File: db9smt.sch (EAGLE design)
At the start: 20 parts, among them CON1 PADONPRINT, CON2 PADONPRINT, CON3 PADONPRINT, CON4 PADONPRINT, CON5 PADONPRINT, CON6 PADONPRINT, CON7 PADONPRINT, CON8 PADONPRINT, CON9 PADONPRINT

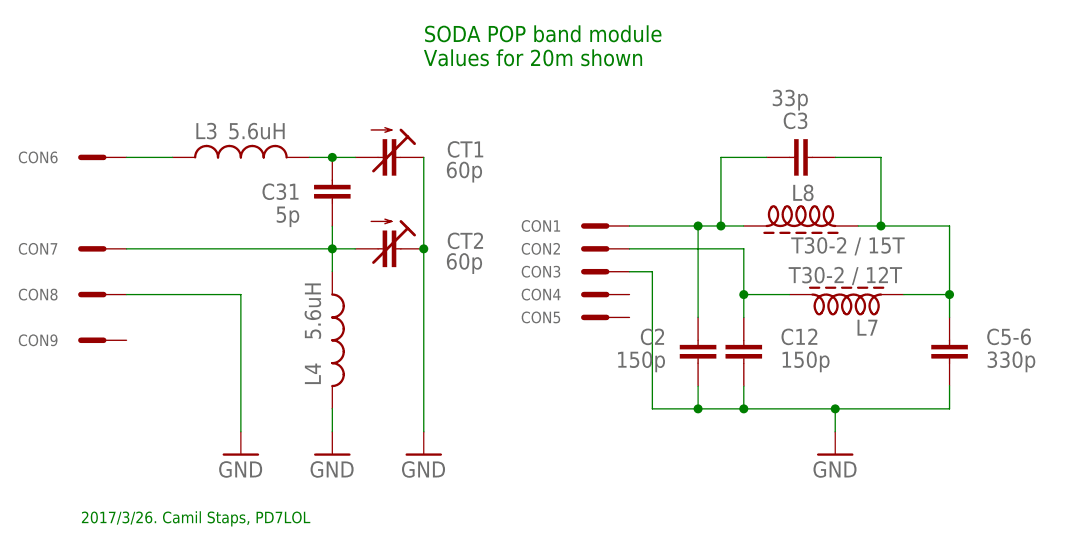
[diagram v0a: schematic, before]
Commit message: GND between signals, remove note space on backside
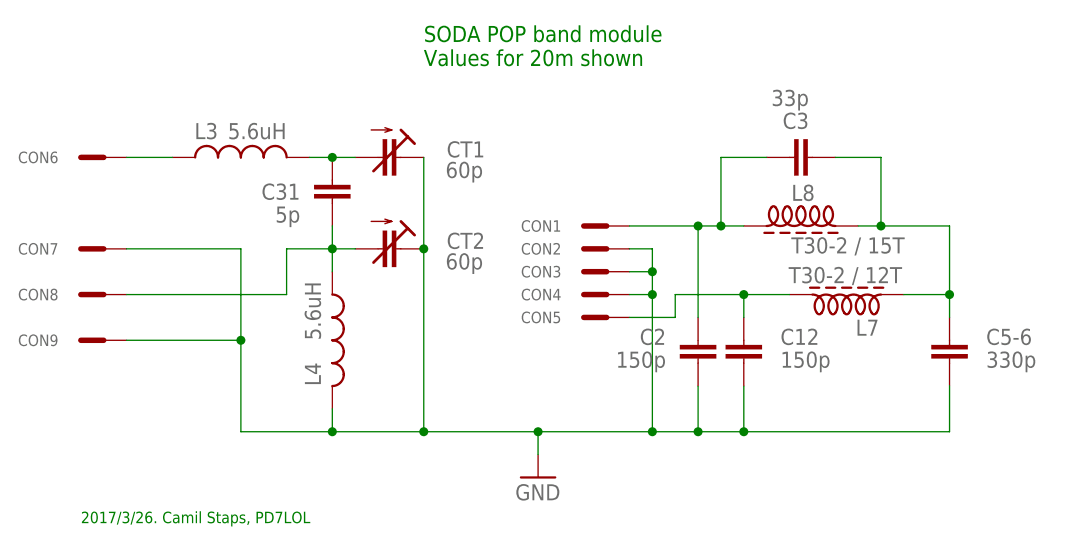
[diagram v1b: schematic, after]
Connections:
- net GND: now also CON2.P$1, CON4.P$1, CON7.P$1, CON9.P$1; no longer CON8.P$1
- net N$1: now also CON8.P$1; no longer CON7.P$1
- net N$5: now also CON5.P$1; no longer CON2.P$1

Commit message: Make DB9 horizontal for smaller footprint and shorter traces
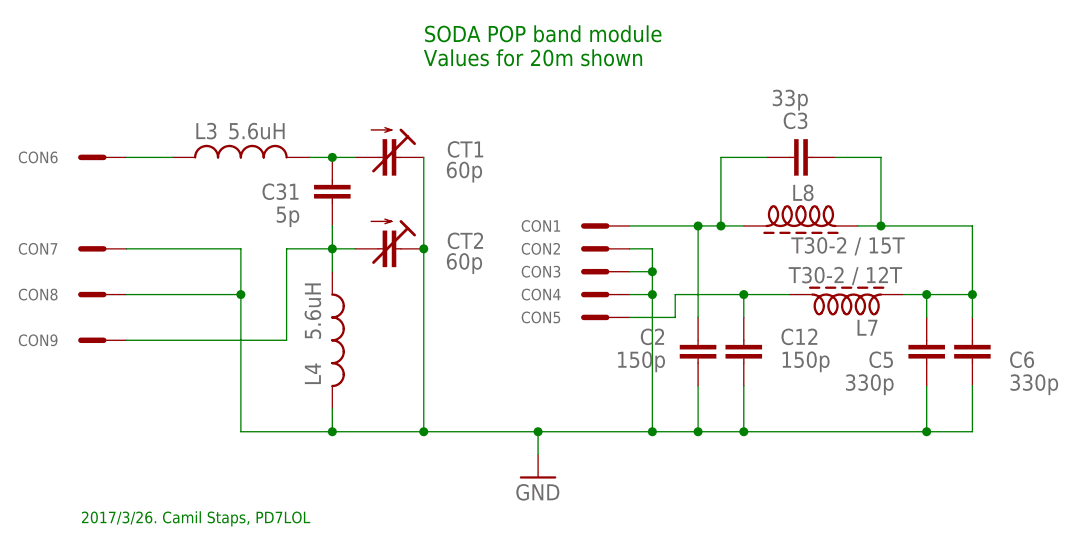
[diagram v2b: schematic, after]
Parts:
- removed C5-6: 330p, eagle-ltspice:CC0603
- added C5, C6: 330p, eagle-ltspice:CC0603
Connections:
- net GND: now also C5.2, C6.2, CON8.P$1; no longer C5-6.2, CON9.P$1
- net N$1: now also CON9.P$1; no longer CON8.P$1
- net N$6: now also C5.1, C6.1; no longer C5-6.1
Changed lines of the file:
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@@
 <part name="C2" library="eagle-ltspice" deviceset="C" device="C0603" value="150p"/>
 <part name="C12" library="eagle-ltspice" deviceset="C" device="C0603" value="150p"/>
-<part name="C5-6" library="eagle-ltspice" deviceset="C" device="C0603" value="330p"/>
+<part name="C6" library="eagle-ltspice" deviceset="C" device="C0603" value="330p"/>
 <part name="C3" library="eagle-ltspice" deviceset="C" device="C0603" value="33p"/>
 <part name="L3" library="rcl" deviceset="L-US" device="L2012C" value="5.6uH"/>
 <part name="L4" library="rcl" deviceset="L-US" device="L2012C" value="5.6uH"/>
 <part name="GND1" library="supply1" deviceset="GND" device=""/>
+<part name="C5" library="eagle-ltspice" deviceset="C" device="C0603" value="330p"/>
 </parts>
 <sheets>
@@
 <attribute name="VALUE" x="11.684" y="43.561" size="1.778" layer="96" align="center-left"/>
 </instance>
-<instance part="C5-6" gate="G$1" x="30.48" y="45.72" smashed="yes">
-<attribute name="NAME" x="34.544" y="46.101" size="1.778" layer="95" align="center-left"/>
-<attribute name="VALUE" x="34.544" y="43.561" size="1.778" layer="96" align="center-left"/>
+<instance part="C6" gate="G$1" x="33.02" y="45.72" smashed="yes">
+<attribute name="NAME" x="37.084" y="43.561" size="1.778" layer="95" align="center-left"/>
+<attribute name="VALUE" x="37.084" y="41.021" size="1.778" layer="96" align="center-left"/>
 </instance>
 <instance part="C3" gate="G$1" x="12.7" y="66.04" smashed="yes" rot="R90">
@@
 </instance>
 <instance part="GND1" gate="1" x="-15.24" y="30.48"/>
+<instance part="C5" gate="G$1" x="27.94" y="45.72" smashed="yes">
+<attribute name="NAME" x="24.384" y="43.561" size="1.778" layer="95" rot="MR0" align="center-left"/>
+<attribute name="VALUE" x="24.384" y="41.021" size="1.778" layer="96" rot="MR0" align="center-left"/>
+</instance>
 </instances>
 <busses>
@@
 <pinref part="L8" gate="G$1" pin="2"/>
 <wire x1="20.32" y1="58.42" x2="22.86" y2="58.42" width="0.1524" layer="91"/>
-<wire x1="22.86" y1="58.42" x2="30.48" y2="58.42" width="0.1524" layer="91"/>
-<wire x1="30.48" y1="58.42" x2="30.48" y2="50.8" width="0.1524" layer="91"/>
-<wire x1="30.48" y1="50.8" x2="30.48" y2="48.26" width="0.1524" layer="91"/>
+<wire x1="22.86" y1="58.42" x2="33.02" y2="58.42" width="0.1524" layer="91"/>
+<wire x1="33.02" y1="58.42" x2="33.02" y2="50.8" width="0.1524" layer="91"/>
+<wire x1="33.02" y1="50.8" x2="33.02" y2="48.26" width="0.1524" layer="91"/>
 <wire x1="17.78" y1="66.04" x2="22.86" y2="66.04" width="0.1524" layer="91"/>
 <wire x1="22.86" y1="66.04" x2="22.86" y2="58.42" width="0.1524" layer="91"/>
 <junction x="22.86" y="58.42"/>
-<junction x="30.48" y="50.8"/>
+<junction x="33.02" y="50.8"/>
 <pinref part="L7" gate="G$1" pin="1"/>
-<wire x1="30.48" y1="50.8" x2="25.4" y2="50.8" width="0.1524" layer="91"/>
-<pinref part="C5-6" gate="G$1" pin="1"/>
+<wire x1="33.02" y1="50.8" x2="27.94" y2="50.8" width="0.1524" layer="91"/>
+<pinref part="C6" gate="G$1" pin="1"/>
 <pinref part="C3" gate="G$1" pin="2"/>
+<pinref part="C5" gate="G$1" pin="1"/>
+<wire x1="27.94" y1="50.8" x2="25.4" y2="50.8" width="0.1524" layer="91"/>
+<wire x1="27.94" y1="48.26" x2="27.94" y2="50.8" width="0.1524" layer="91"/>
+<junction x="27.94" y="50.8"/>
 </segment>
 </net>
@@
 <wire x1="-38.1" y1="55.88" x2="-38.1" y2="53.34" width="0.1524" layer="91"/>
 <wire x1="-38.1" y1="55.88" x2="-43.18" y2="55.88" width="0.1524" layer="91"/>
-<pinref part="CON8" gate="G$1" pin="P$1"/>
-<wire x1="-60.96" y1="50.8" x2="-43.18" y2="50.8" width="0.1524" layer="91"/>
-<wire x1="-43.18" y1="50.8" x2="-43.18" y2="55.88" width="0.1524" layer="91"/>
+<wire x1="-43.18" y1="55.88" x2="-43.18" y2="45.72" width="0.1524" layer="91"/>
+<pinref part="CON9" gate="G$1" pin="P$1"/>
+<wire x1="-43.18" y1="45.72" x2="-60.96" y2="45.72" width="0.1524" layer="91"/>
 </segment>
 </net>
 <net name="GND" class="0">
 <segment>
-<wire x1="-48.26" y1="55.88" x2="-48.26" y2="45.72" width="0.1524" layer="91"/>
 <pinref part="CON7" gate="G$1" pin="P$1"/>
-<wire x1="-48.26" y1="45.72" x2="-48.26" y2="35.56" width="0.1524" layer="91"/>
+<wire x1="-48.26" y1="55.88" x2="-48.26" y2="50.8" width="0.1524" layer="91"/>
+<wire x1="-48.26" y1="50.8" x2="-48.26" y2="35.56" width="0.1524" layer="91"/>
 <wire x1="-60.96" y1="55.88" x2="-48.26" y2="55.88" width="0.1524" layer="91"/>
-<pinref part="CON9" gate="G$1" pin="P$1"/>
-<wire x1="-60.96" y1="45.72" x2="-48.26" y2="45.72" width="0.1524" layer="91"/>
-<junction x="-48.26" y="45.72"/>
 <pinref part="L4" gate="G$1" pin="2"/>
 <wire x1="-38.1" y1="38.1" x2="-38.1" y2="35.56" width="0.1524" layer="91"/>
@@
 <wire x1="-2.54" y1="53.34" x2="-2.54" y2="50.8" width="0.1524" layer="91"/>
 <wire x1="-2.54" y1="50.8" x2="-2.54" y2="35.56" width="0.1524" layer="91"/>
-<pinref part="C5-6" gate="G$1" pin="2"/>
+<pinref part="C6" gate="G$1" pin="2"/>
 <pinref part="CON2" gate="G$1" pin="P$1"/>
 <wire x1="-5.08" y1="55.88" x2="-2.54" y2="55.88" width="0.1524" layer="91"/>
@@
 <wire x1="7.62" y1="35.56" x2="2.54" y2="35.56" width="0.1524" layer="91"/>
 <junction x="2.54" y="35.56"/>
-<wire x1="7.62" y1="35.56" x2="30.48" y2="35.56" width="0.1524" layer="91"/>
-<wire x1="30.48" y1="35.56" x2="30.48" y2="40.64" width="0.1524" layer="91"/>
+<wire x1="7.62" y1="35.56" x2="27.94" y2="35.56" width="0.1524" layer="91"/>
+<wire x1="27.94" y1="35.56" x2="33.02" y2="35.56" width="0.1524" layer="91"/>
+<wire x1="33.02" y1="35.56" x2="33.02" y2="40.64" width="0.1524" layer="91"/>
 <junction x="7.62" y="35.56"/>
+<pinref part="CON8" gate="G$1" pin="P$1"/>
+<wire x1="-60.96" y1="50.8" x2="-48.26" y2="50.8" width="0.1524" layer="91"/>
+<junction x="-48.26" y="50.8"/>
+<pinref part="C5" gate="G$1" pin="2"/>
+<wire x1="27.94" y1="40.64" x2="27.94" y2="35.56" width="0.1524" layer="91"/>
+<junction x="27.94" y="35.56"/>
 </segment>
 </net>
@@
 </sheet>
 </sheets>
-<errors>
-</errors>
 </schematic>
 </drawing>

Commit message: Move TX lines on DB9 connector
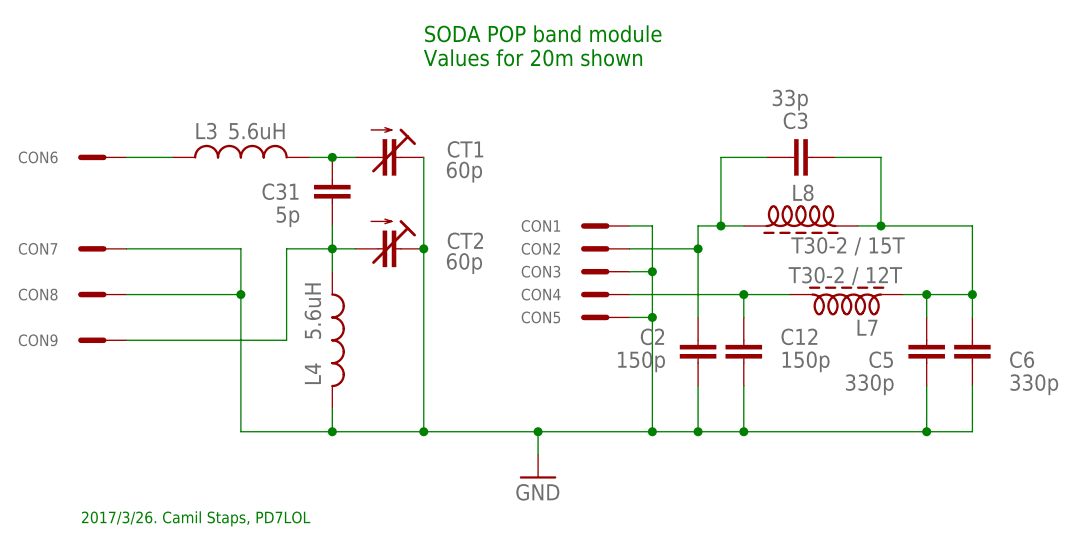
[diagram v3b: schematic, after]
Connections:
- net GND: now also CON1.P$1, CON5.P$1; no longer CON2.P$1, CON4.P$1
- net N$4: now also CON2.P$1; no longer CON1.P$1
- net N$5: now also CON4.P$1; no longer CON5.P$1
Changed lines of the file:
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@@
 <pinref part="L8" gate="G$1" pin="1"/>
 <wire x1="7.62" y1="58.42" x2="5.08" y2="58.42" width="0.1524" layer="91"/>
-<wire x1="2.54" y1="48.26" x2="2.54" y2="58.42" width="0.1524" layer="91"/>
+<wire x1="2.54" y1="48.26" x2="2.54" y2="55.88" width="0.1524" layer="91"/>
+<wire x1="2.54" y1="55.88" x2="2.54" y2="58.42" width="0.1524" layer="91"/>
 <wire x1="2.54" y1="58.42" x2="5.08" y2="58.42" width="0.1524" layer="91"/>
 <wire x1="5.08" y1="58.42" x2="5.08" y2="66.04" width="0.1524" layer="91"/>
@@
 <pinref part="C2" gate="G$1" pin="1"/>
 <pinref part="C3" gate="G$1" pin="1"/>
-<pinref part="CON1" gate="G$1" pin="P$1"/>
-<wire x1="2.54" y1="58.42" x2="-5.08" y2="58.42" width="0.1524" layer="91"/>
-<junction x="2.54" y="58.42"/>
+<pinref part="CON2" gate="G$1" pin="P$1"/>
+<wire x1="-5.08" y1="55.88" x2="2.54" y2="55.88" width="0.1524" layer="91"/>
+<junction x="2.54" y="55.88"/>
 </segment>
 </net>
@@
 <wire x1="12.7" y1="50.8" x2="7.62" y2="50.8" width="0.1524" layer="91"/>
 <pinref part="C12" gate="G$1" pin="1"/>
-<wire x1="7.62" y1="50.8" x2="0" y2="50.8" width="0.1524" layer="91"/>
-<wire x1="0" y1="50.8" x2="0" y2="48.26" width="0.1524" layer="91"/>
+<wire x1="7.62" y1="50.8" x2="-5.08" y2="50.8" width="0.1524" layer="91"/>
 <junction x="7.62" y="50.8"/>
-<pinref part="CON5" gate="G$1" pin="P$1"/>
-<wire x1="0" y1="48.26" x2="-5.08" y2="48.26" width="0.1524" layer="91"/>
+<pinref part="CON4" gate="G$1" pin="P$1"/>
 </segment>
 </net>
@@
 <pinref part="CON3" gate="G$1" pin="P$1"/>
 <wire x1="-5.08" y1="53.34" x2="-2.54" y2="53.34" width="0.1524" layer="91"/>
-<wire x1="-2.54" y1="53.34" x2="-2.54" y2="50.8" width="0.1524" layer="91"/>
-<wire x1="-2.54" y1="50.8" x2="-2.54" y2="35.56" width="0.1524" layer="91"/>
+<wire x1="-2.54" y1="53.34" x2="-2.54" y2="48.26" width="0.1524" layer="91"/>
 <pinref part="C6" gate="G$1" pin="2"/>
-<pinref part="CON2" gate="G$1" pin="P$1"/>
-<wire x1="-5.08" y1="55.88" x2="-2.54" y2="55.88" width="0.1524" layer="91"/>
-<wire x1="-2.54" y1="55.88" x2="-2.54" y2="53.34" width="0.1524" layer="91"/>
-<junction x="-2.54" y="53.34"/>
-<pinref part="CON4" gate="G$1" pin="P$1"/>
-<wire x1="-5.08" y1="50.8" x2="-2.54" y2="50.8" width="0.1524" layer="91"/>
-<junction x="-2.54" y="50.8"/>
+<wire x1="-2.54" y1="48.26" x2="-2.54" y2="35.56" width="0.1524" layer="91"/>
 <wire x1="-15.24" y1="35.56" x2="-2.54" y2="35.56" width="0.1524" layer="91"/>
 <junction x="-15.24" y="35.56"/>
@@
 <wire x1="27.94" y1="40.64" x2="27.94" y2="35.56" width="0.1524" layer="91"/>
 <junction x="27.94" y="35.56"/>
+<pinref part="CON5" gate="G$1" pin="P$1"/>
+<wire x1="-5.08" y1="48.26" x2="-2.54" y2="48.26" width="0.1524" layer="91"/>
+<junction x="-2.54" y="48.26"/>
+<pinref part="CON1" gate="G$1" pin="P$1"/>
+<wire x1="-5.08" y1="58.42" x2="-2.54" y2="58.42" width="0.1524" layer="91"/>
+<wire x1="-2.54" y1="58.42" x2="-2.54" y2="53.34" width="0.1524" layer="91"/>
+<junction x="-2.54" y="53.34"/>
 </segment>
 </net>
